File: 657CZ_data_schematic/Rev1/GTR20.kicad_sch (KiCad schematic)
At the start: 1 part

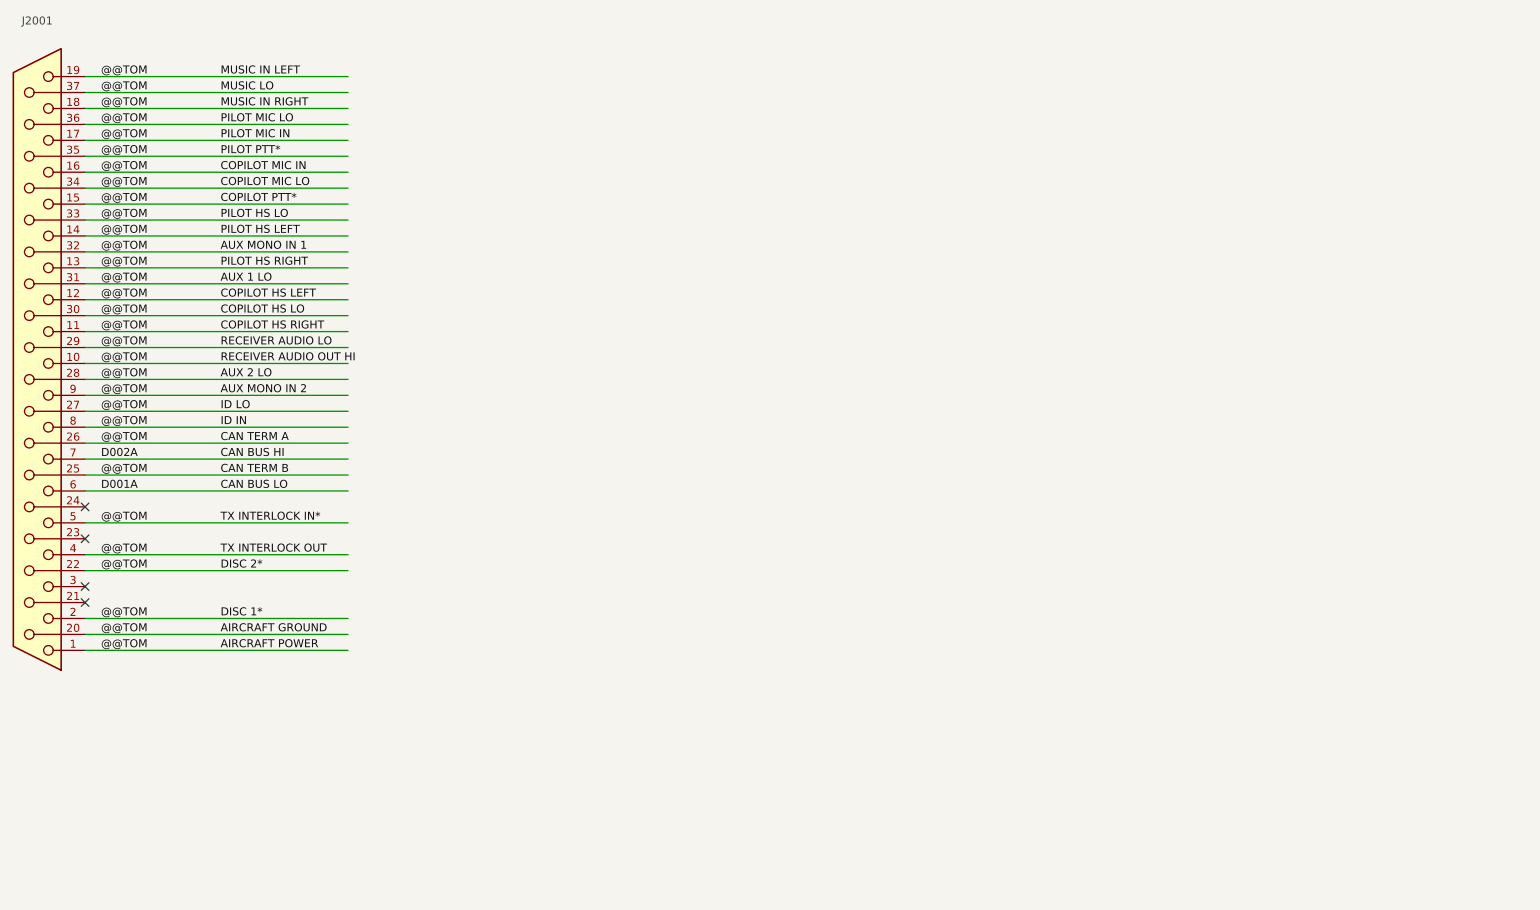
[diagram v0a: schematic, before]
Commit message: added data connections after AvClassics wiring. completed LRUs GMU, GDU, GSU, GAD, GNC, GTX, GTR  Not completed GMA, GEA and autopilot LRUs
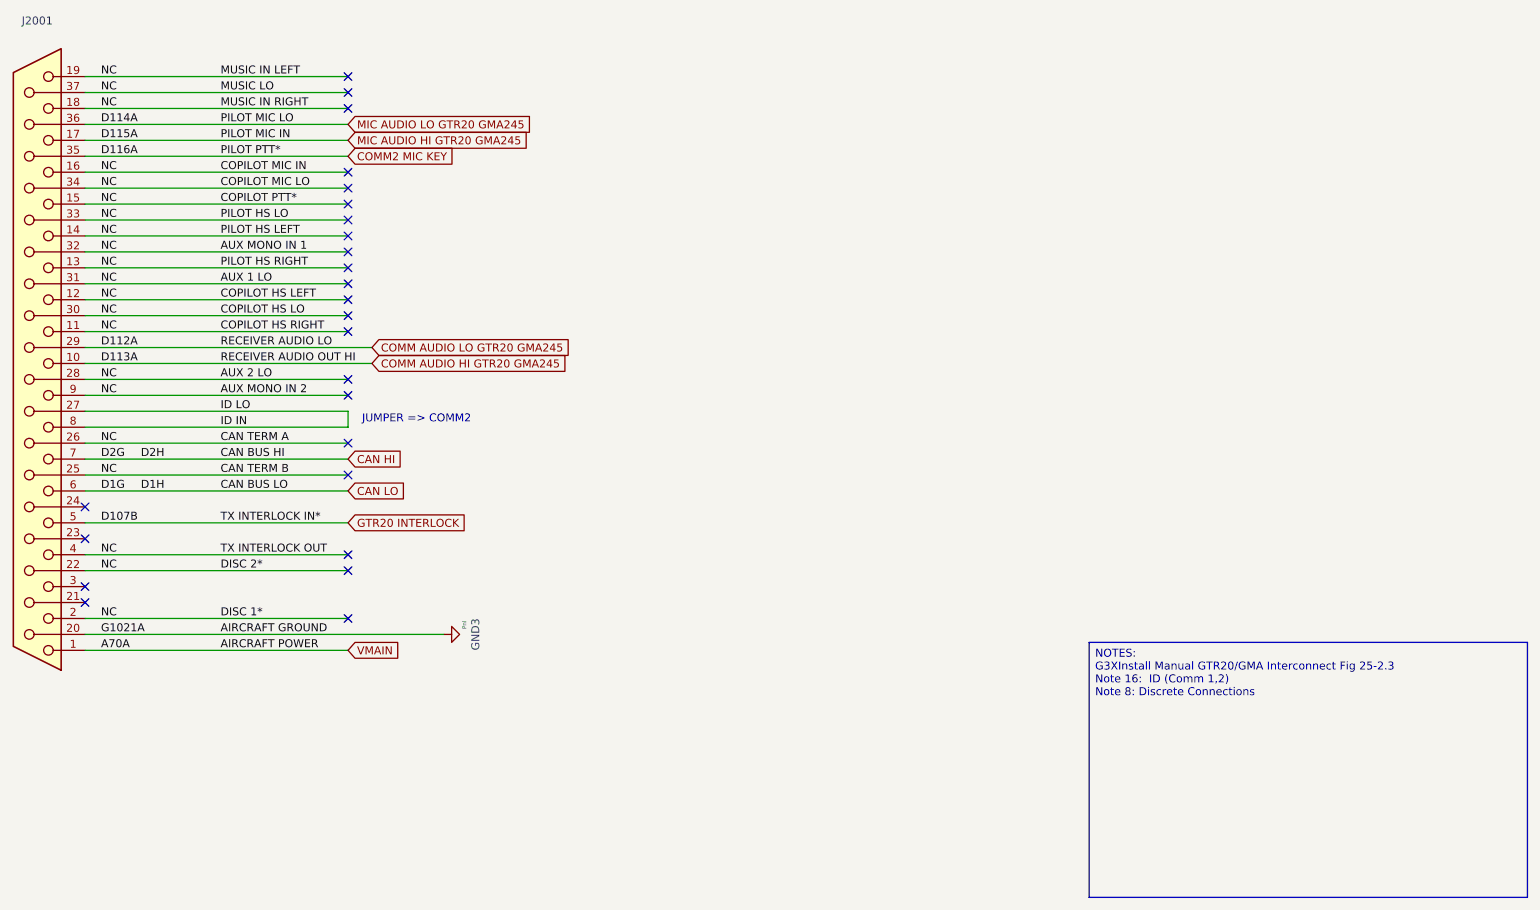
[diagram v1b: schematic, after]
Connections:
- net @@TOM renamed AUX 1 LO
- net AUX 1 LO: no longer J2001.1, J2001.10, J2001.17 (11), J2001.20 (P14), J2001.27 (P21), J2001.29 (P23), J2001.35 (P23), J2001.36 (P24), J2001.5, J2001.8
- net CAN BUS HI renamed CAN HI
- net CAN BUS LO renamed CAN LO
- new net COMM AUDIO HI GTR20 GMA245: J2001.10
- new net COMM AUDIO LO GTR20 GMA245: J2001.29 (P23)
- new net COMM2 MIC KEY: J2001.35 (P23)
- new net GND3: J2001.20 (P14)
- new net GTR20 INTERLOCK: J2001.5
- new net ID IN: J2001.27 (P21), J2001.8
- new net MIC AUDIO HI GTR20 GMA245: J2001.17 (11)
- new net MIC AUDIO LO GTR20 GMA245: J2001.36 (P24)
- new net VMAIN: J2001.1
- no-connect marks 4 -> 25
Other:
- note added: "JUMPER => COMM2"
